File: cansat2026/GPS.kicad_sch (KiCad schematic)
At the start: 12 parts, among them J801 Conn_Coaxial, U801 NEO-M9N

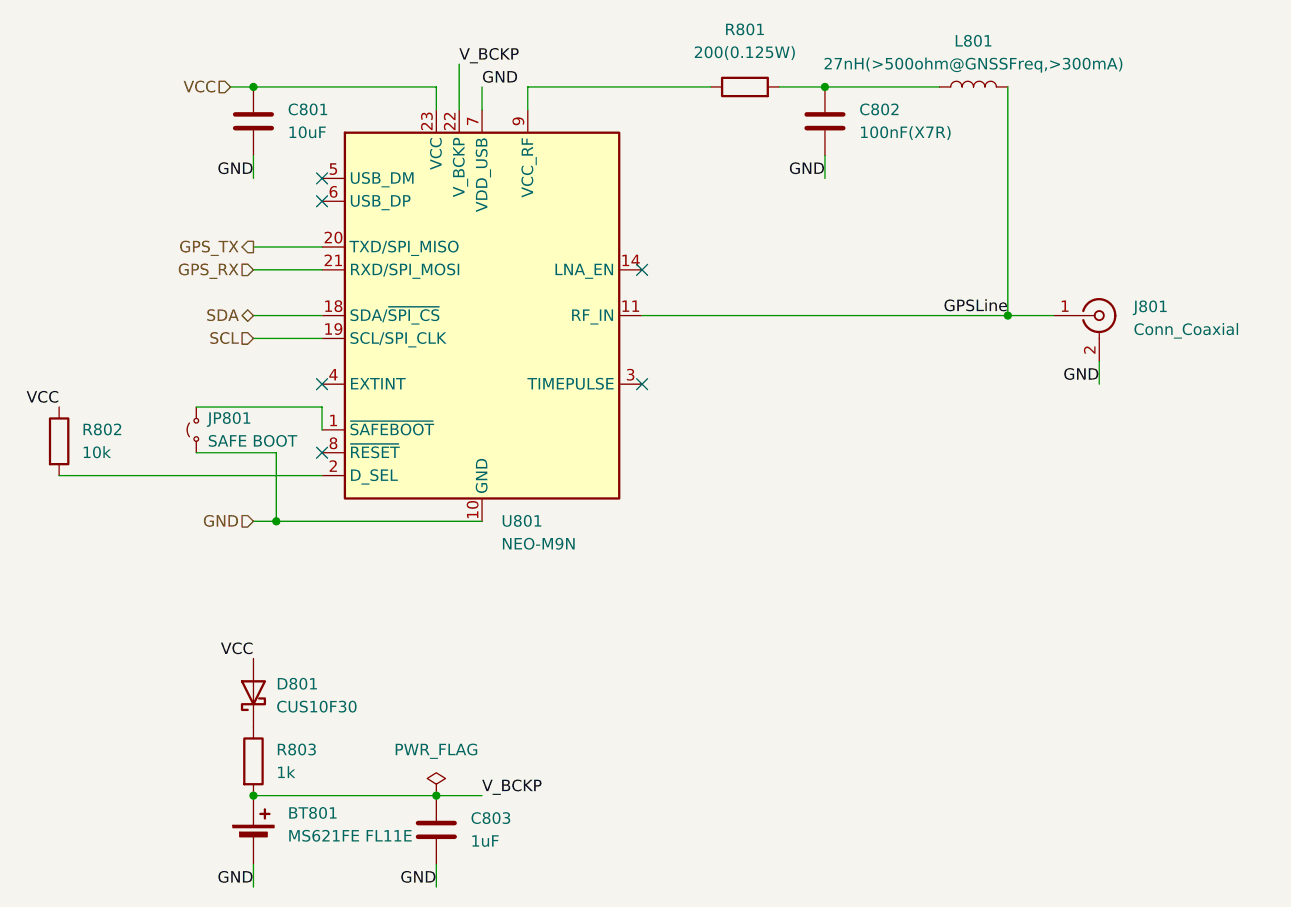
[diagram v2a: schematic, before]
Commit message: Update: いろいろした
GPS変えた
USB追加した
気圧センサ変えた
FPGA変えた
MDにキャパシタ追加した
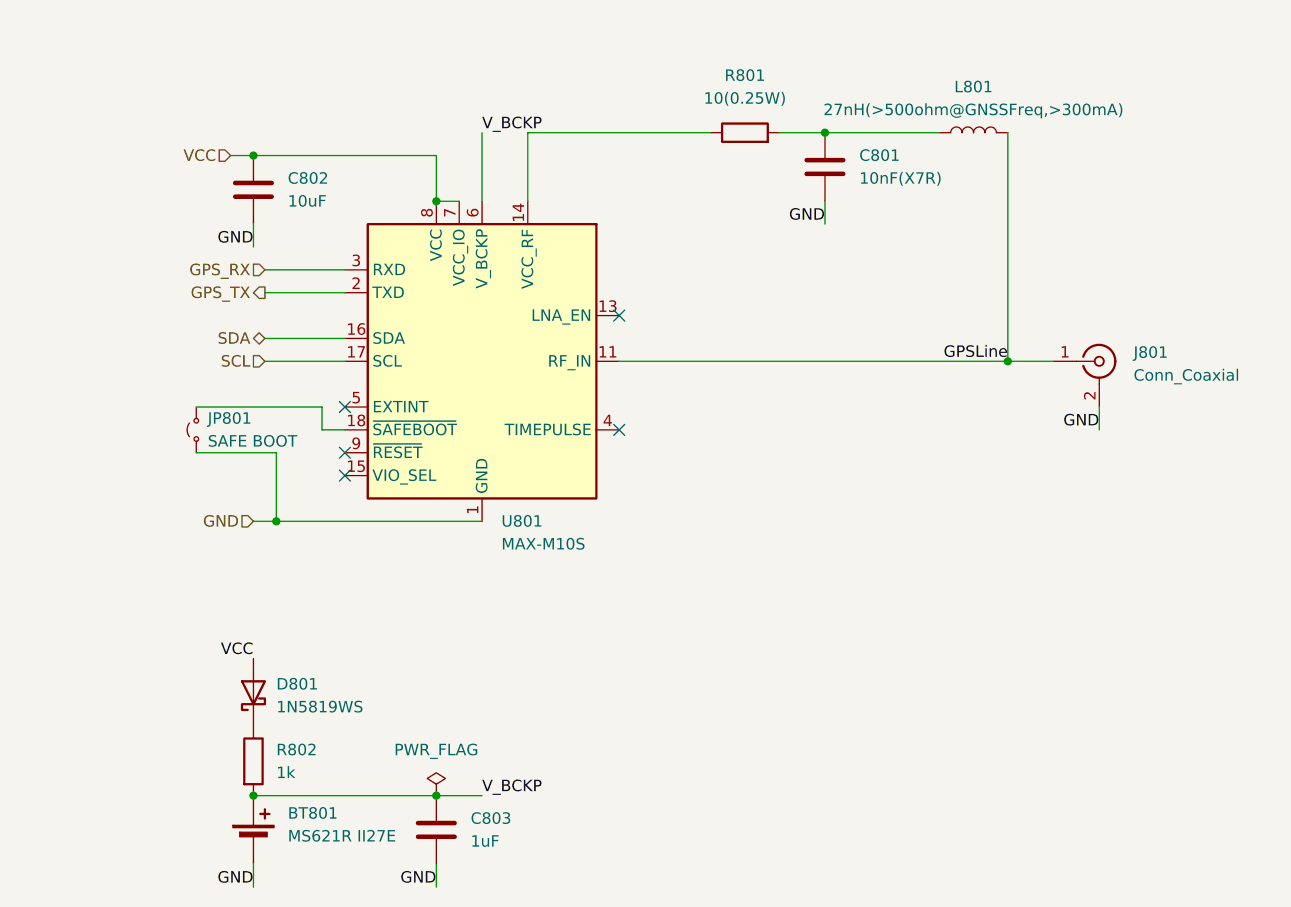
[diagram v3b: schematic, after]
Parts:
- removed R802: 10k, Resistor_SMD:R_0402_1005Metric, symbol Device:R
- removed U801: NEO-M9N, RF_GPS:ublox_NEO, symbol RF_GPS:NEO-M9N
- added U801: MAX-M10S, RF_GPS:ublox_MAX, symbol RF_GPS:MAX-M10S
- BT801: value MS621FE FL11E -> MS621R II27E; footprint Battery:BatteryHolder_Seiko_MS621F -> Project:BAT_MS621R-II27E
- C801: renamed from C802; value 100nF(X7R) -> 10nF(X7R); LCSC Part C1525 -> C15195
- D801: value CUS10F30 -> 1N5819WS; LCSC Part (none) -> C191023
- R801: value 200(0.125W) -> 10(0.25W); footprint Resistor_SMD:R_0805_2012Metric -> Resistor_SMD:R_1206_3216Metric; LCSC Part C17540 -> C17903
- renumbered C801 to C802, R803 to R802
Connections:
- net GND: now also U801.1 (GND), U801.10 (GND), U801.12 (GND)
- net GPSLine: now also U801.11 (RF_IN)
- net GPS_RX: now also U801.3 (RXD)
- net GPS_TX: now also U801.2 (TXD)
- net SCL: now also U801.17 (SCL)
- net SDA: now also U801.16 (SDA)
- net VCC: now also U801.7 (VCC_IO), U801.8 (VCC)
- net V_BCKP: now also U801.6 (V_BCKP)
- net at JP801.2 (B): now also U801.18 (~{SAFEBOOT})
- net at R801.1: now also U801.14 (VCC_RF)
- no-connect marks 6 -> 5
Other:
- moved on the sheet: C801, C802, J801, L801, R801

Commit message: Update: 完成した
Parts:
- BT801: 秋月 Part (none) -> 117518
- J801: footprint Connector_Coaxial:SMA_Amphenol_132134-11_Vertical -> Connector_Coaxial:U.FL_Hirose_U.FL-R-SMT-1_Vertical; 秋月 Part (none) -> 115417
- JP801: now left out of the parts list
- L801: DigiKey Part (none) -> LQW18AN27NG00D; Mouser Part 710-7447860127G -> (none)
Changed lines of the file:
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@@
 			)
 		)
-		(property "Mouser Part" "710-7447860127G"
+		(property "Mouser Part" ""
 			(at 194.31 81.28 90)
 			(hide yes)
@@
 			)
 		)
-		(property "DigiKey Part" ""
+		(property "DigiKey Part" "LQW18AN27NG00D"
 			(at 194.31 81.28 90)
 			(hide yes)
@@
 			)
 		)
+		(property "秋月 Part" "117518"
+			(at 114.3 160.02 0)
+			(hide yes)
+			(show_name no)
+			(do_not_autoplace no)
+			(effects
+				(font
+					(size 1.27 1.27)
+				)
+			)
+		)
 		(pin "1"
 		)
@@
 			)
 		)
-		(property "Footprint" "Connector_Coaxial:SMA_Amphenol_132134-11_Vertical"
+		(property "Footprint" "Connector_Coaxial:U.FL_Hirose_U.FL-R-SMT-1_Vertical"
 			(at 208.28 106.68 0)
 			(hide yes)
@@
 		)
 		(property "DigiKey Part" ""
+			(at 208.28 106.68 0)
+			(hide yes)
+			(show_name no)
+			(do_not_autoplace no)
+			(effects
+				(font
+					(size 1.27 1.27)
+				)
+			)
+		)
+		(property "秋月 Part" "115417"
 			(at 208.28 106.68 0)
 			(hide yes)
@@
 		(body_style 1)
 		(exclude_from_sim no)
-		(in_bom yes)
+		(in_bom no)
 		(on_board yes)
 		(in_pos_files yes)
